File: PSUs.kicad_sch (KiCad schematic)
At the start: 33 parts, among them J6 Barrel_Jack, J7 AMP171826-4, U4 AP64501SP-13

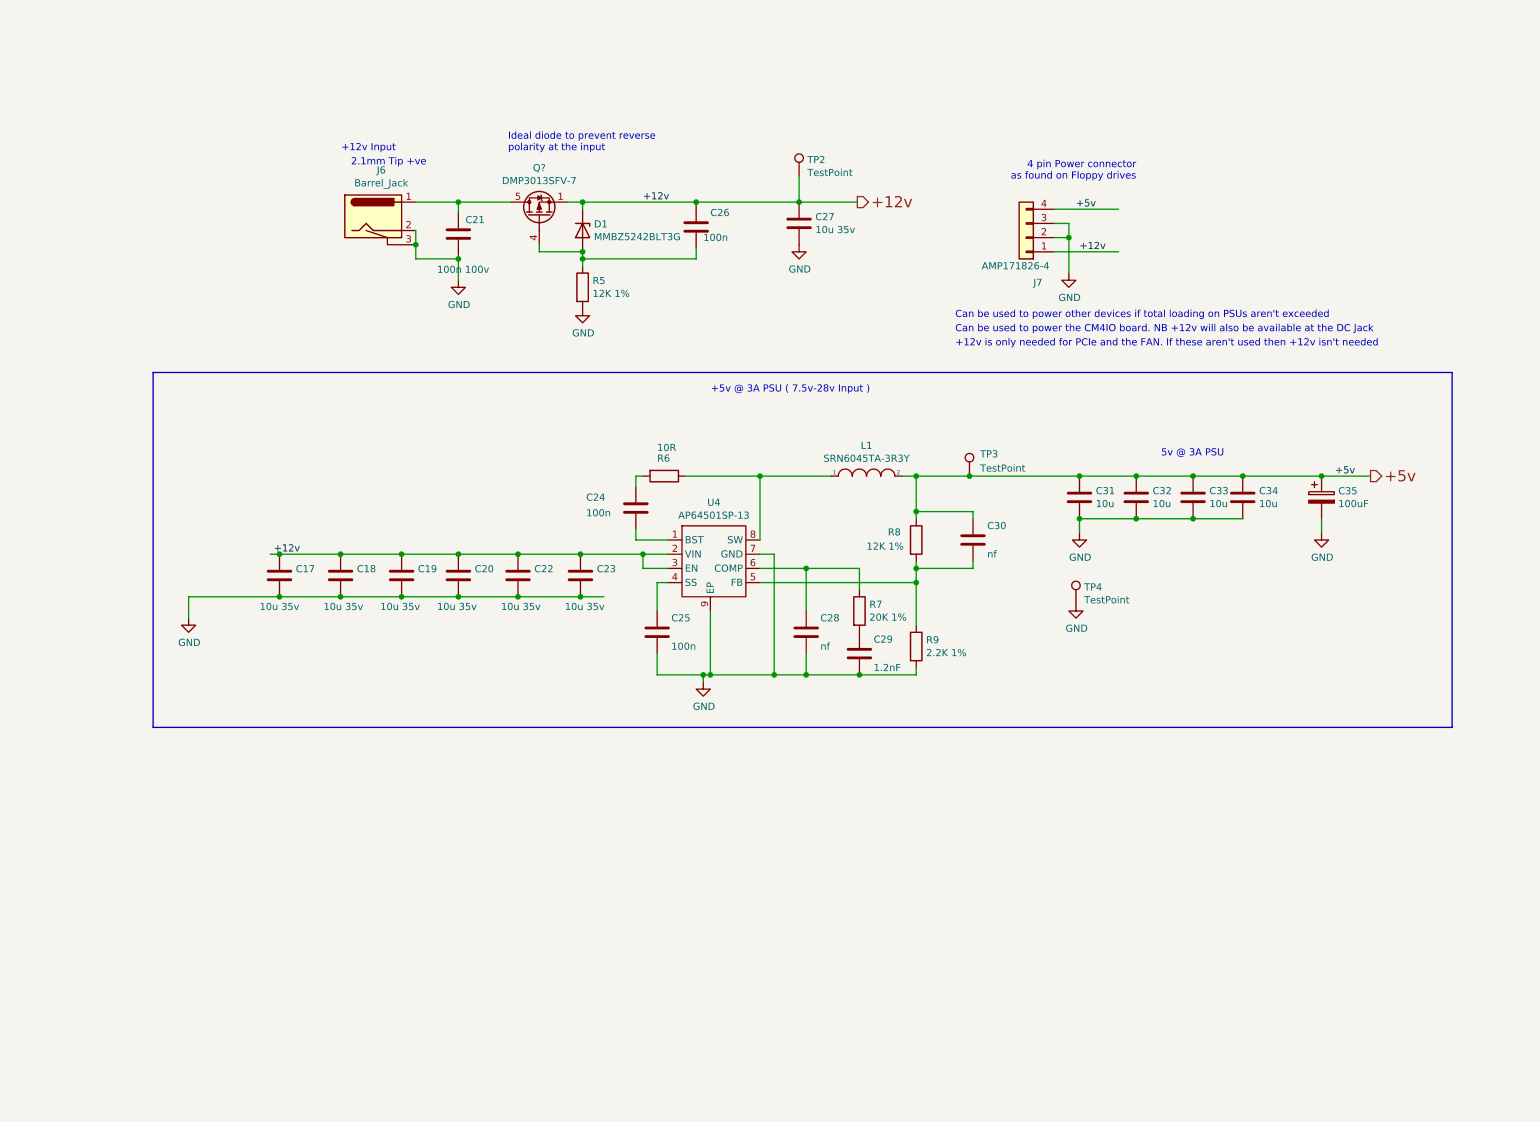
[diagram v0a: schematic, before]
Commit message: Moved PCIe psu to global psu schematic
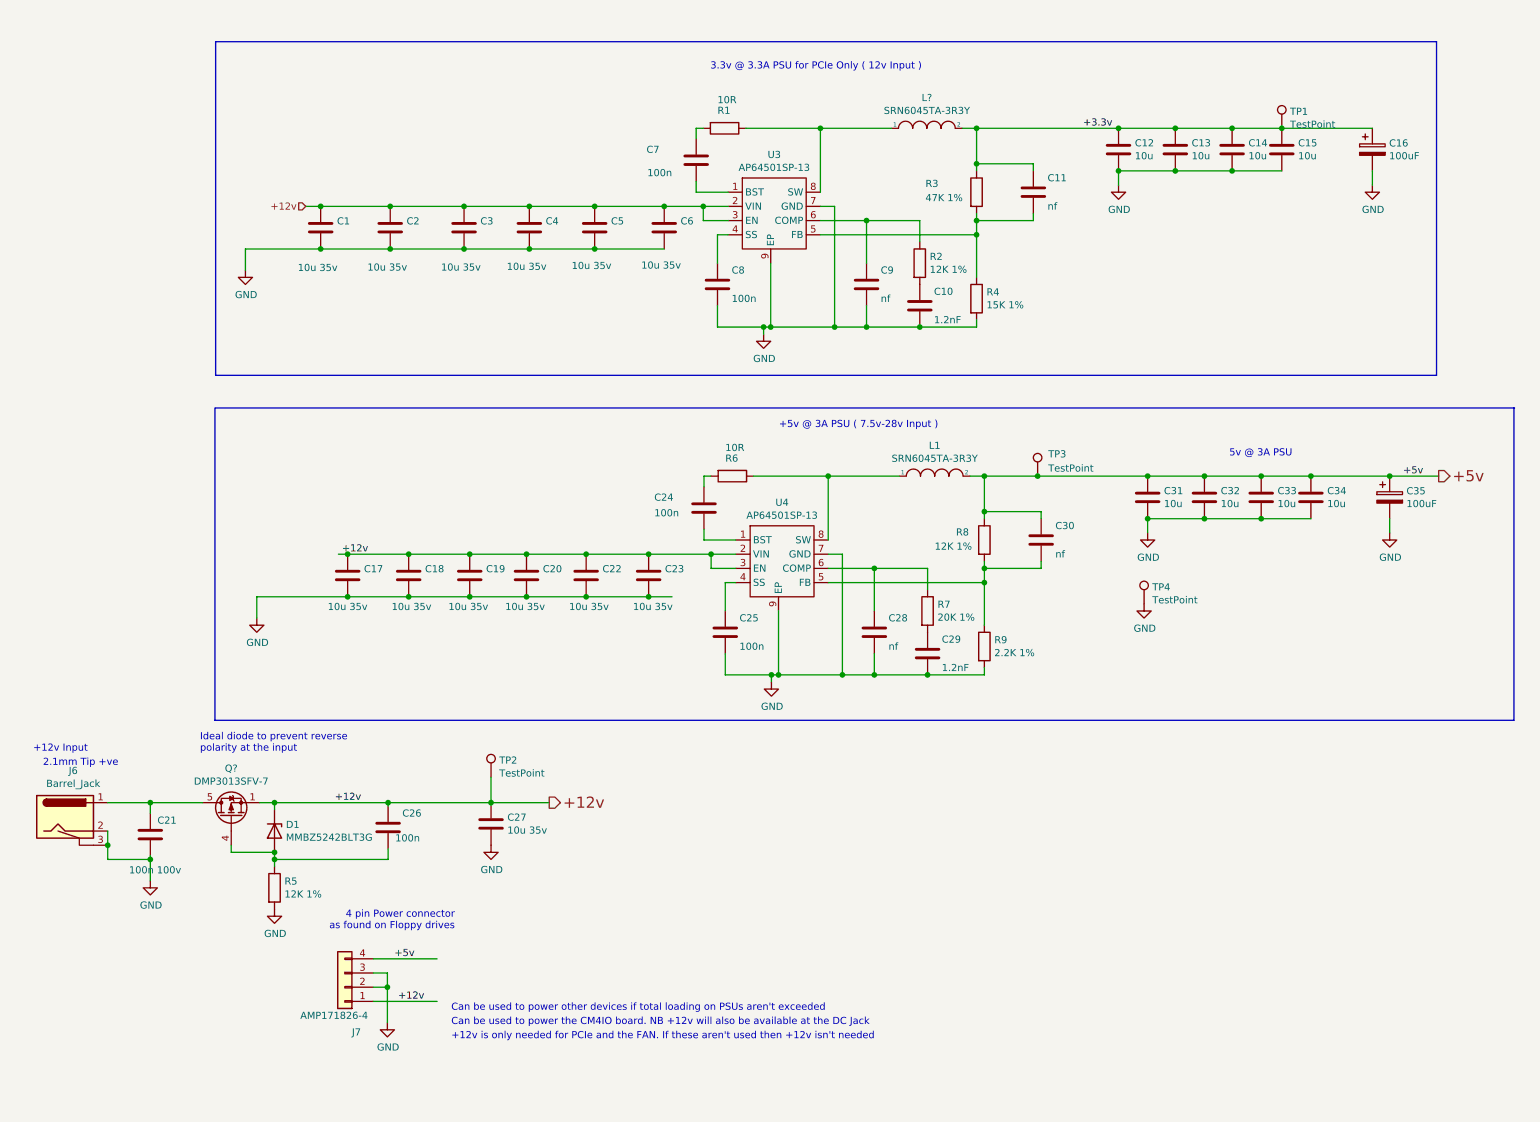
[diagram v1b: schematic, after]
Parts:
- added C1, C2, C3, C4, C5, C6: 10u 35v, Capacitor_SMD:C_0805_2012Metric, symbol Device:C
- added C10: 1.2nF, Capacitor_SMD:C_0402_1005Metric, symbol Device:C
- added C11, C9: nf, Capacitor_SMD:C_0402_1005Metric, symbol Device:C
- added C12, C13, C14, C15: 10u, Capacitor_SMD:C_0805_2012Metric, symbol Device:C
- added C16: 100uF, Capacitor_Tantalum_SMD:CP_EIA-7343-31_Kemet-D, symbol Device:CP
- added C7, C8: 100n, Capacitor_SMD:C_0402_1005Metric, symbol Device:C
- added L?: SRN6045TA-3R3Y, Inductor_SMD:L_Bourns_SRN6045TA, symbol pspice:INDUCTOR
- added R1: 10R, Resistor_SMD:R_0402_1005Metric, symbol Device:R
- added R2: 12K 1%, Resistor_SMD:R_0402_1005Metric, symbol Device:R
- added R3: 47K 1%, Resistor_SMD:R_0402_1005Metric, symbol Device:R
- added R4: 15K 1%, Resistor_SMD:R_0402_1005Metric, symbol Device:R
- added TP1: TestPoint, TestPoint:TestPoint_Pad_2.0x2.0mm, symbol Connector:TestPoint
- added U3: AP64501SP-13, CM4IO:SOIC-8-1EP_3.9x4.9mm_P1.27mm_EP2.95x4.9mm_Mask2.71x3.4mm_ThermalVias, symbol CM4IO:AP64351
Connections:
- net +12v: now also C1.1, C2.1, C3.1, C4.1, C5.1, C6.1, U3.2 (VIN), U3.3 (EN)
- net GND: now also C1.2, C10.2, C12.2, C13.2, C14.2, C15.2, C16.2, C2.2, C3.2, C4.2, C5.2, C6.2, C8.2, C9.2, R4.2, U3.7 (GND), U3.9 (EP)
- new net: L?.1, R1.1, U3.8 (SW)
- new net: C9.1, R2.1, U3.6 (COMP)
- new net: C10.1, R2.2
- new net: C11.2, R3.2, R4.1, U3.5 (FB)
- new net: C8.1, U3.4 (SS)
- new net: C7.2, U3.1 (BST)
- new net: C7.1, R1.2
- new net +3.3v: C11.1, C12.1, C13.1, C14.1, C15.1, C16.1, L?.2, R3.1, TP1.1
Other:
- note added: "3.3v @ 3.3A PSU for PCIe Only ( 12v Input )"
- moved on the sheet: C17, C18, C19, C20, C21, C22, C23, C24, C25, C26, C27, C28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

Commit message: Cleaned up schematics and added gnds and no-connects
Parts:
- added U8: AP62300WU-7, AP62300WU-7:SOT95P280X100-6N, symbol AP62300WU-7:AP62300WU-7
- gave numbers to parts that had none: 2
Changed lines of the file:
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@@
 		(on_board yes)
 		(dnp no)
-		(property "Reference" "L?"
+		(property "Reference" "L2"
 			(at 173.99 27.559 0)
 			(effects
@@
 			(project "ANE21_PCB"
 				(path "/27bae9d5-8d47-4d02-9c9d-2650041a529b/1710a55d-c4fa-4b6a-99e2-6054aab87aa6"
-					(reference "L?")
+					(reference "L2")
 					(unit 1)
 				)
@@
 		(on_board yes)
 		(dnp no)
-		(property "Reference" "Q?"
+		(property "Reference" "Q1"
 			(at 49.53 147.5486 90)
 			(effects
@@
 			(project "ANE21_PCB"
 				(path "/27bae9d5-8d47-4d02-9c9d-2650041a529b/1710a55d-c4fa-4b6a-99e2-6054aab87aa6"
-					(reference "Q?")
+					(reference "Q1")
 					(unit 1)
 				)
@@
 					(unit 1)
 				)
+			)
+		)
+	)
+	(symbol
+		(lib_id "AP62300WU-7:AP62300WU-7")
+		(at 97.79 95.25 0)
+		(unit 1)
+		(exclude_from_sim no)
+		(in_bom yes)
+		(on_board yes)
+		(dnp no)
+		(fields_autoplaced yes)
+		(property "Reference" "U8"
+			(at 97.79 82.55 0)
+			(effects
+				(font
+					(size 1.27 1.27)
+				)
+			)
+		)
+		(property "Value" "AP62300WU-7"
+			(at 97.79 85.09 0)
+			(effects
+				(font
+					(size 1.27 1.27)
+				)
+			)
+		)
+		(property "Footprint" "AP62300WU-7:SOT95P280X100-6N"
+			(at 97.79 95.25 0)
+			(effects
+				(font
+					(size 1.27 1.27)
+				)
+				(justify bottom)
+				(hide yes)
+			)
+		)
+		(property "Datasheet" ""
+			(at 97.79 95.25 0)
+			(effects
+				(font
+					(size 1.27 1.27)
+				)
+				(hide yes)
+			)
+		)
+		(property "Description" ""
+			(at 97.79 95.25 0)
+			(effects
+				(font
+					(size 1.27 1.27)
+				)
+				(hide yes)
+			)
+		)
+		(property "DigiKey_Part_Number" "31-AP62300WU-7CT-ND"
+			(at 97.79 95.25 0)
+			(effects
+				(font
+					(size 1.27 1.27)
+				)
+				(justify bottom)
+				(hide yes)
+			)
+		)
+		(property "SnapEDA_Link" "https://www.snapeda.com/parts/AP62300WU-7/Diodes+Inc./view-part/?ref=snap"
+			(at 97.79 95.25 0)
+			(effects
+				(font
+					(size 1.27 1.27)
+				)
+				(justify bottom)
+				(hide yes)
+			)
+		)
+		(property "MAXIMUM_PACKAGE_HEIGHT" "1.0mm"
+			(at 97.79 95.25 0)
+			(effects
+				(font
+					(size 1.27 1.27)
+				)
+				(justify bottom)
+				(hide yes)
+			)
+		)
+		(property "Package" "None"
+			(at 97.79 95.25 0)
+			(effects
+				(font
+					(size 1.27 1.27)
+				)
+				(justify bottom)
+				(hide yes)
+			)
+		)
+		(property "Check_prices" "https://www.snapeda.com/parts/AP62300WU-7/Diodes+Inc./view-part/?ref=eda"
+			(at 97.79 95.25 0)
+			(effects
+				(font
+					(size 1.27 1.27)
+				)
+				(justify bottom)
+				(hide yes)
+			)
+		)
+		(property "STANDARD" "IPC 7351B"
+			(at 97.79 95.25 0)
+			(effects
+				(font
+					(size 1.27 1.27)
+				)
+				(justify bottom)
+				(hide yes)
+			)
+		)
+		(property "PARTREV" "Rev. 3 - 2"
+			(at 97.79 95.25 0)
+			(effects
+				(font
+					(size 1.27 1.27)
+				)
+				(justify bottom)
+				(hide yes)
+			)
+		)
+		(property "MF" "Diodes Incorporated"
+			(at 97.79 95.25 0)
+			(effects
+				(font
+					(size 1.27 1.27)
+				)
+				(justify bottom)
+				(hide yes)
+			)
+		)
+		(property "MP" "AP62300WU-7"
+			(at 97.79 95.25 0)
+			(effects
+				(font
+					(size 1.27 1.27)
+				)
+				(justify bottom)
+				(hide yes)
+			)
+		)
+		(property "Description_1" "Buck Switching Regulator IC Positive Adjustable 0.8V 1 Output 3A SOT-23-6 Thin, TSOT-23-6"
+			(at 97.79 95.25 0)
+			(effects
+				(font
+					(size 1.27 1.27)
+				)
+				(justify bottom)
+				(hide yes)
+			)
+		)
+		(property "SNAPEDA_PN" "AP62300TWU-7"
+			(at 97.79 95.25 0)
+			(effects
+				(font
+					(size 1.27 1.27)
+				)
+				(justify bottom)
+				(hide yes)
+			)
+		)
+		(property "MANUFACTURER" "Diodes Inc."
+			(at 97.79 95.25 0)
+			(effects
+				(font
+					(size 1.27 1.27)
+				)
+				(justify bottom)
+				(hide yes)
+			)
+		)
+		(pin "3"
+		)
+		(pin "5"
+		)
+		(pin "4"
+		)
+		(pin "2"
+		)
+		(pin "6"
+		)
+		(pin "1"
+		)
+		(instances
+			(project ""
+				(path "/27bae9d5-8d47-4d02-9c9d-2650041a529b/1710a55d-c4fa-4b6a-99e2-6054aab87aa6"
+					(reference "U8")
+					(unit 1)
+				)
